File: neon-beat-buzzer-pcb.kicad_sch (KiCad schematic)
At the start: 66 parts, among them J1 BATT_CON, J2 SWITCH_CON, J3 BUTTON_CON, J4 USB_C_Receptacle_USB2.0_16P, U1 ESP32-C3-MINI-1, U2 BQ24074RGT, U3 TPS22929D, U4 74AHCT1G125, U5 TPS610997DRV, U6 USBLC6-2SC6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

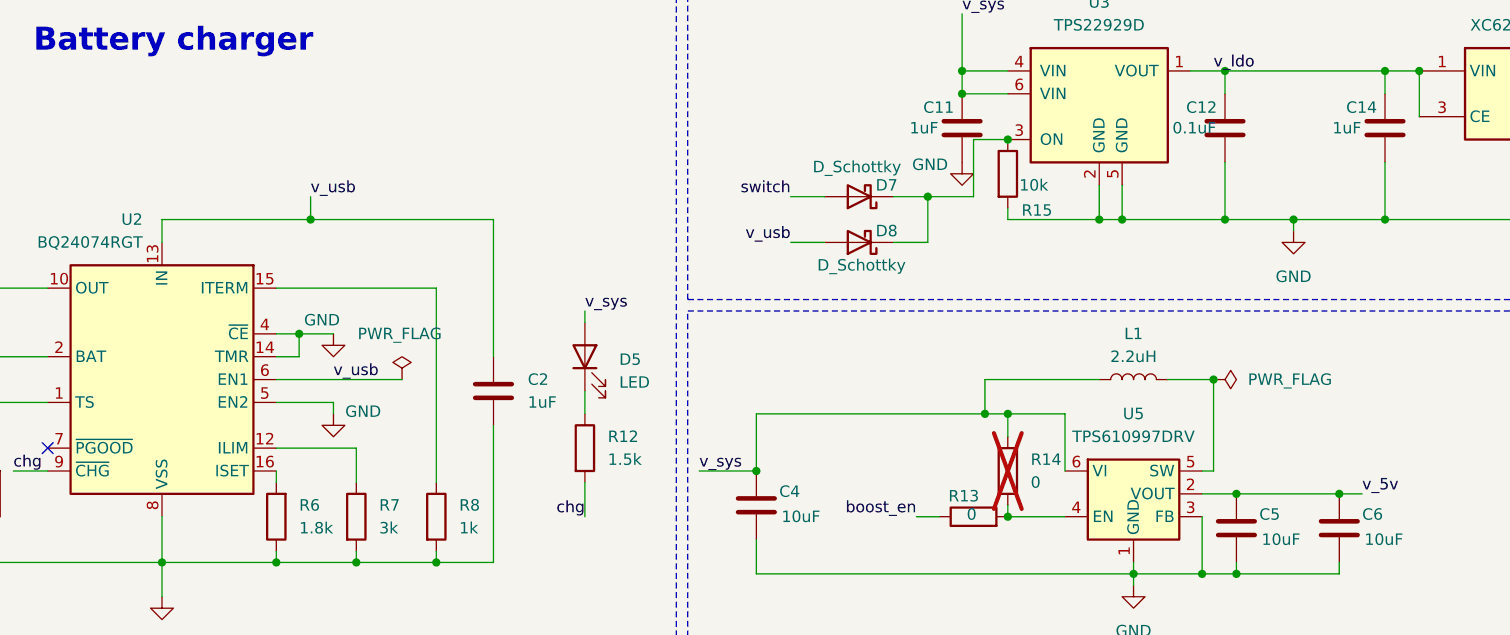
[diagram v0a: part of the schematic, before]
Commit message: pcb: a few adjustments
Mostly setting a few power sources on the schematic

Signed-off-by: Alexis Lothoré <alexis.lothore@gmail.com>
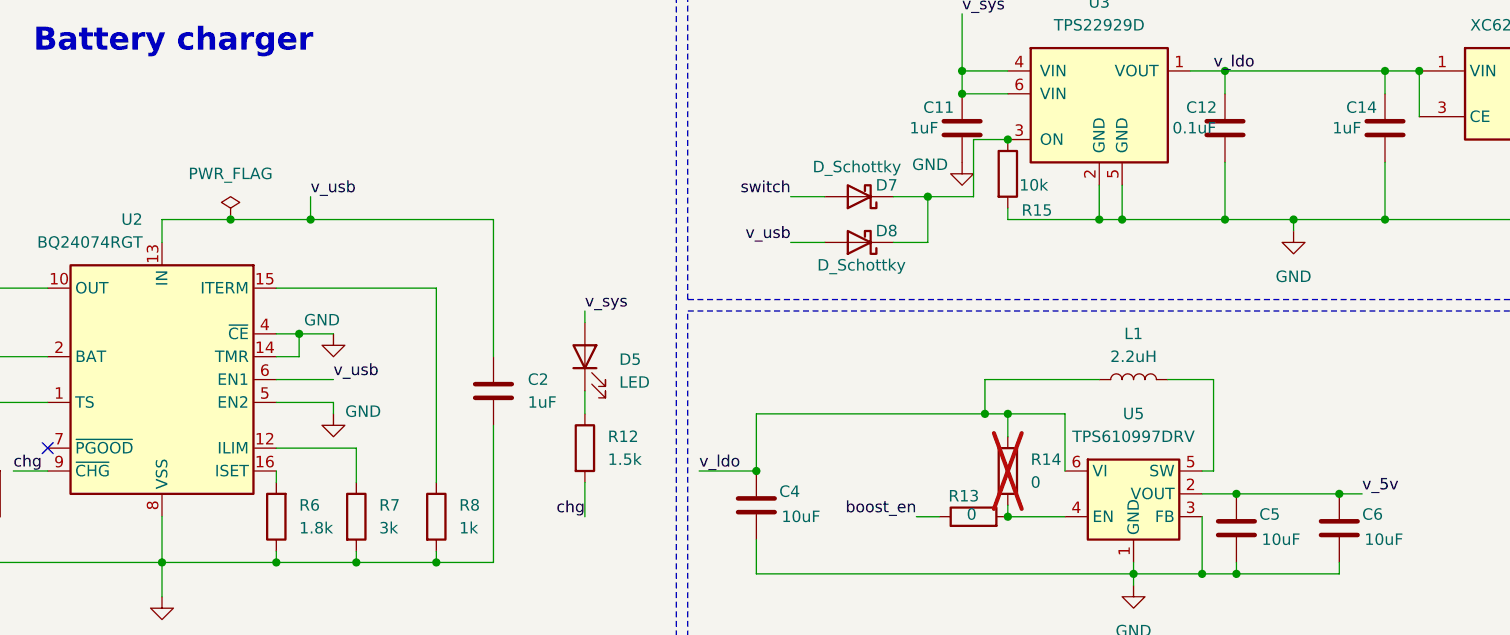
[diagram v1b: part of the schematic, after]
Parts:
- D5: footprint Diode_SMD:D_0805_2012Metric_Pad1.15x1.40mm_HandSolder -> LED_SMD:LED_0603_1608Metric
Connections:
- net v_ldo: now also C4.1, L1.2, R14.2, U5.6 (VI)
- net v_sys: no longer C4.1, L1.2, R14.2, U5.6 (VI)
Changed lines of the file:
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@@
 	)
 	(junction
-		(at 179.07 59.69)
-		(diameter 0)
-		(color 0 0 0 0)
-	)
-	(junction
 		(at 198.12 25.4)
 		(diameter 0)
@@
 	)
 	(junction
+		(at 69.85 41.91)
+		(diameter 0)
+		(color 0 0 0 0)
+	)
+	(junction
 		(at 147.32 39.37)
 		(diameter 0)
@@
 	(wire
 		(pts
+			(xy 74.93 59.69) (xy 81.28 59.69)
+		)
+		(stroke
+			(width 0)
+			(type default)
+		)
+	)
+	(wire
+		(pts
 			(xy 26.67 179.07) (xy 34.29 179.07)
 		)
@@
 	(wire
 		(pts
+			(xy 69.85 41.91) (xy 62.23 41.91)
+		)
+		(stroke
+			(width 0)
+			(type default)
+		)
+	)
+	(wire
+		(pts
 			(xy 177.8 74.93) (xy 177.8 81.28)
 		)
@@
 	(wire
 		(pts
-			(xy 78.74 41.91) (xy 62.23 41.91)
+			(xy 78.74 41.91) (xy 69.85 41.91)
 		)
 		(stroke
@@
 	(wire
 		(pts
-			(xy 74.93 59.69) (xy 88.9 59.69)
-		)
-		(stroke
-			(width 0)
-			(type default)
-		)
-	)
-	(wire
-		(pts
 			(xy 266.7 78.74) (xy 269.24 78.74)
 		)
@@
 		)
 	)
-	(label "v_sys"
+	(label "v_ldo"
 		(at 121.92 69.85 0)
 		(effects
@@
 	)
 	(symbol
-		(lib_id "power:PWR_FLAG")
-		(at 88.9 59.69 0)
-		(unit 1)
-		(body_style 1)
-		(exclude_from_sim no)
-		(in_bom yes)
-		(on_board yes)
-		(in_pos_files yes)
-		(dnp no)
-		(property "Reference" "#FLG02"
-			(at 88.9 57.785 0)
-			(hide yes)
-			(show_name no)
-			(do_not_autoplace no)
-			(effects
-				(font
-					(size 1.27 1.27)
-				)
-			)
-		)
-		(property "Value" "PWR_FLAG"
-			(at 88.646 54.61 0)
-			(show_name no)
-			(do_not_autoplace no)
-			(effects
-				(font
-					(size 1.27 1.27)
-				)
-			)
-		)
-		(property "Footprint" ""
-			(at 88.9 59.69 0)
-			(hide yes)
-			(show_name no)
-			(do_not_autoplace no)
-			(effects
-				(font
-					(size 1.27 1.27)
-				)
-			)
-		)
-		(property "Datasheet" ""
-			(at 88.9 59.69 0)
-			(hide yes)
-			(show_name no)
-			(do_not_autoplace no)
-			(effects
-				(font
-					(size 1.27 1.27)
-				)
-			)
-		)
-		(property "Description" "Special symbol for telling ERC where power comes from"
-			(at 88.9 59.69 0)
-			(hide yes)
-			(show_name no)
-			(do_not_autoplace no)
-			(effects
-				(font
-					(size 1.27 1.27)
-				)
-			)
-		)
-		(pin "1"
-		)
-		(instances
-			(project "neon-beat-buzzer-pcb"
-				(path "/1aa5bb6d-1502-4465-bf5e-41cf5ab51d4a"
-					(reference "#FLG02")
-					(unit 1)
-				)
-			)
-		)
-	)
-	(symbol
 		(lib_id "Battery_Management:BQ24074RGT")
 		(at 62.23 59.69 0)
@@
 	)
 	(symbol
+		(lib_id "power:PWR_FLAG")
+		(at 69.85 41.91 0)
+		(unit 1)
+		(body_style 1)
+		(exclude_from_sim no)
+		(in_bom yes)
+		(on_board yes)
+		(in_pos_files yes)
+		(dnp no)
+		(fields_autoplaced yes)
+		(property "Reference" "#FLG04"
+			(at 69.85 40.005 0)
+			(hide yes)
+			(show_name no)
+			(do_not_autoplace no)
+			(effects
+				(font
+					(size 1.27 1.27)
+				)
+			)
+		)
+		(property "Value" "PWR_FLAG"
+			(at 69.85 36.83 0)
+			(show_name no)
+			(do_not_autoplace no)
+			(effects
+				(font
+					(size 1.27 1.27)
+				)
+			)
+		)
+		(property "Footprint" ""
+			(at 69.85 41.91 0)
+			(hide yes)
+			(show_name no)
+			(do_not_autoplace no)
+			(effects
+				(font
+					(size 1.27 1.27)
+				)
+			)
+		)
+		(property "Datasheet" ""
+			(at 69.85 41.91 0)
+			(hide yes)
+			(show_name no)
+			(do_not_autoplace no)
+			(effects
+				(font
+					(size 1.27 1.27)
+				)
+			)
+		)
+		(property "Description" "Special symbol for telling ERC where power comes from"
+			(at 69.85 41.91 0)
+			(hide yes)
+			(show_name no)
+			(do_not_autoplace no)
+			(effects
+				(font
+					(size 1.27 1.27)
+				)
+			)
+		)
+		(pin "1"
+		)
+		(instances
+			(project "neon-beat-buzzer-pcb"
+				(path "/1aa5bb6d-1502-4465-bf5e-41cf5ab51d4a"
+					(reference "#FLG04")
+					(unit 1)
+				)
+			)
+		)
+	)
+	(symbol
 		(lib_id "Mechanical:MountingHole_Pad")
 		(at 251.46 151.13 0)
@@
 	)
 	(symbol
-		(lib_id "power:PWR_FLAG")
-		(at 179.07 59.69 270)
-		(unit 1)
-		(body_style 1)
-		(exclude_from_sim no)
-		(in_bom yes)
-		(on_board yes)
-		(in_pos_files yes)
-		(dnp no)
-		(fields_autoplaced yes)
-		(property "Reference" "#FLG03"
-			(at 180.975 59.69 0)
-			(hide yes)
-			(show_name no)
-			(do_not_autoplace no)
-			(effects
-				(font
-					(size 1.27 1.27)
-				)
-			)
-		)
-		(property "Value" "PWR_FLAG"
-			(at 182.88 59.6899 90)
-			(show_name no)
-			(do_not_autoplace no)
-			(effects
-				(font
-					(size 1.27 1.27)
-				)
-				(justify left)
-			)
-		)
-		(property "Footprint" ""
-			(at 179.07 59.69 0)
-			(hide yes)
-			(show_name no)
-			(do_not_autoplace no)
-			(effects
-				(font
-					(size 1.27 1.27)
-				)
-			)
-		)
-		(property "Datasheet" ""
-			(at 179.07 59.69 0)
-			(hide yes)
-			(show_name no)
-			(do_not_autoplace no)
-			(effects
-				(font
-					(size 1.27 1.27)
-				)
-			)
-		)
-		(property "Description" "Special symbol for telling ERC where power comes from"
-			(at 179.07 59.69 0)
-			(hide yes)
-			(show_name no)
-			(do_not_autoplace no)
-			(effects
-				(font
-					(size 1.27 1.27)
-				)
-			)
-		)
-		(pin "1"
-		)
-		(instances
-			(project "neon-beat-buzzer-pcb"
-				(path "/1aa5bb6d-1502-4465-bf5e-41cf5ab51d4a"
-					(reference "#FLG03")
-					(unit 1)
-				)
-			)
-		)
-	)
-	(symbol
 		(lib_id "power:GND")
 		(at 200.66 116.84 0)
@@
 			)
 		)
-		(property "Footprint" "Diode_SMD:D_0805_2012Metric_Pad1.15x1.40mm_HandSolder"
+		(property "Footprint" "LED_SMD:LED_0603_1608Metric"
 			(at 109.22 57.15 0)
 			(hide yes)
